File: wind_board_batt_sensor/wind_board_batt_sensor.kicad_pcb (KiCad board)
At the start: 2 copper layers, 82.4 x 23.5 mm, 35 parts, among them J1 Batt +, J2 Batt -, J3 Sys +, J4 Sys -, U1 MAX17263xxTE, U2 PTSM82903SISB2R, U3 ATtiny402-SS

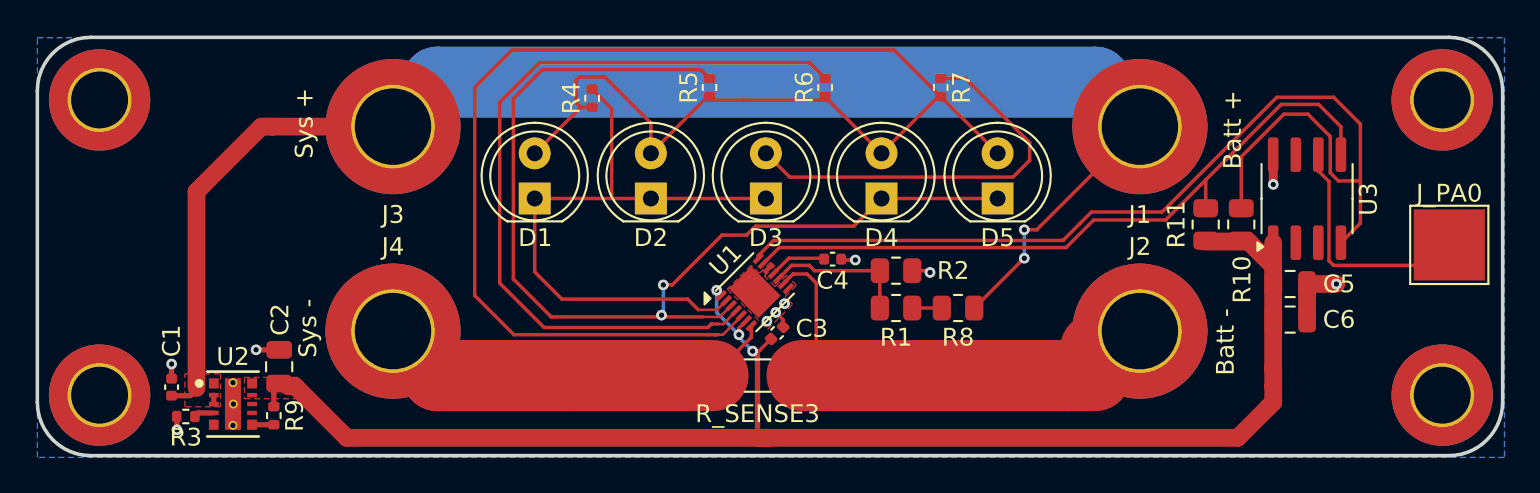
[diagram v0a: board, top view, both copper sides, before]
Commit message: All components to 0805 on battery board
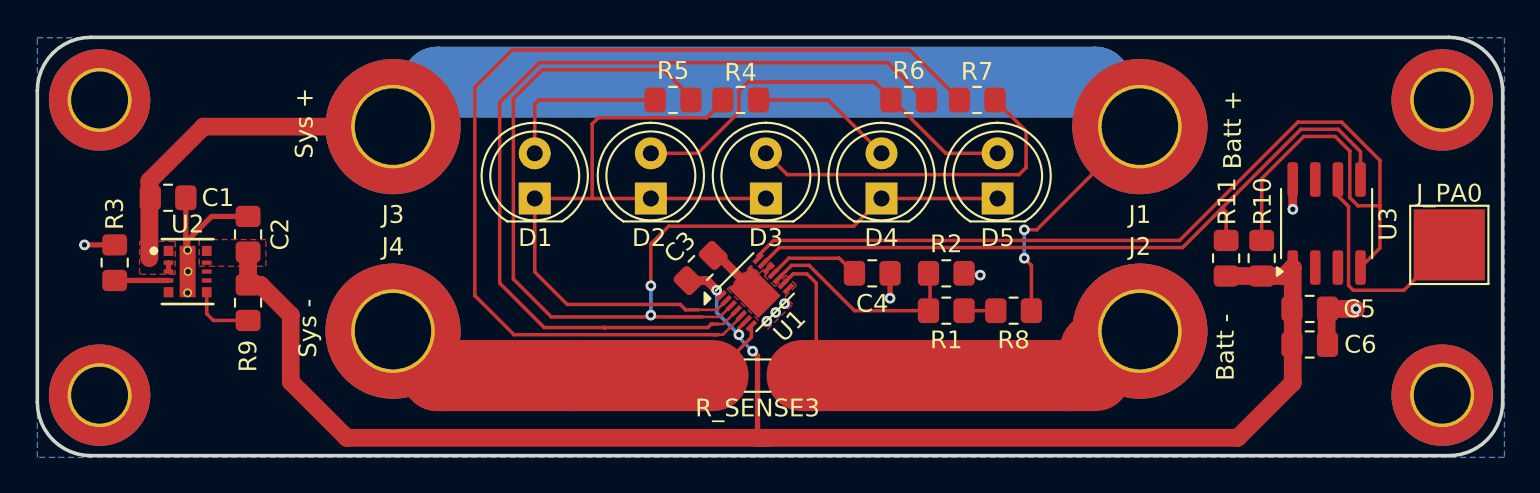
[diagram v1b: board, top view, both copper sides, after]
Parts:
- C1, C3, C4: footprint Capacitor_SMD:C_0402_1005Metric -> Resistor_SMD:R_0805_2012Metric_Pad1.20x1.40mm_HandSolder
- C2, C5, C6: footprint Capacitor_SMD:C_0805_2012Metric -> Resistor_SMD:R_0805_2012Metric_Pad1.20x1.40mm_HandSolder
- R1, R10, R11, R2, R8: footprint Resistor_SMD:R_0805_2012Metric -> Resistor_SMD:R_0805_2012Metric_Pad1.20x1.40mm_HandSolder
- R3, R4, R5, R6, R7, R9: footprint Resistor_SMD:R_0402_1005Metric -> Resistor_SMD:R_0805_2012Metric_Pad1.20x1.40mm_HandSolder
- R_SENSE3: footprint Resistor_SMD:R_1206_3216Metric -> Resistor_SMD:R_1206_3216Metric_Pad1.30x1.75mm_HandSolder
- moved C1 10.7 mm to (95.3, 99.0), turned to 0 degrees
- moved R3 9.53 mm to (92.3, 102.7), turned to 90 degrees
- moved R4 8.35 mm to (127.5, 93.5), turned to 180 degrees
- moved U2 7.87 mm to (96.5, 103.2)
- moved C2 7.65 mm to (99.8, 101.0)
- moved R9 6.51 mm to (99.8, 104.9)
- moved C3 5.64 mm to (125.3, 103.0)
- moved R6 4.75 mm to (137.0, 93.5), turned to 0 degrees
- moved R8 3.13 mm to (142.9, 105.3)
- moved R1 2.83 mm to (139.1, 105.3)
- moved R2 2.83 mm to (139.1, 103.3)
- moved C4 2.37 mm to (134.9, 103.2)
- moved R10 2.22 mm to (156.8, 102.4)
- moved R11 2.22 mm to (154.8, 102.4)
- moved R5 2.17 mm to (123.8, 93.5), turned to 0 degrees
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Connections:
- D2 pad 2: Net-(D1-A) -> Net-(D2-A)
- D4 pad 2: Net-(D1-A) -> Net-(D4-A)
- D5 pad 2: Net-(D1-A) -> Net-(D2-A)
- R4 pad 1: Net-(D1-A) -> Net-(D4-A)
- R6 pad 1: Net-(D1-A) -> Net-(D2-A)
- R7 pad 2: Net-(D1-A) -> Net-(U1-L4)
- U1 pad 5: Net-(D1-A) -> Net-(U1-L4)
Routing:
- net Net-(D1-A): track 93.8 -> 10.0 mm
- net Net-(U1-L4): track 0.00 -> 57.9 mm
- net Net-(D2-A): track 0.00 -> 23.5 mm
- net ~: track 39.2 -> 48.2 mm, vias 10 -> 8
- net Net-(D4-A): track 0.00 -> 8.31 mm
- net +3.3V: track 84.1 -> 90.8 mm
- net Net-(J1-Pin_1): track 84.3 -> 77.9 mm
- net Net-(U1-L3): track 44.5 -> 50.8 mm
- net Net-(D1-K): track 35.8 -> 41.2 mm
- net Net-(D3-A): track 23.3 -> 19.8 mm
- net Net-(U1-CELLX/CSPH): track 8.69 -> 11.9 mm
- net Net-(U2-PG): track 1.23 -> 3.69 mm
- net Net-(U1-REG): track 3.23 -> 5.27 mm
- net Net-(U2-MODE_S-CONF): track 1.15 -> 3.03 mm
- net Net-(U1-SCL): track 58.8 -> 60.5 mm
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
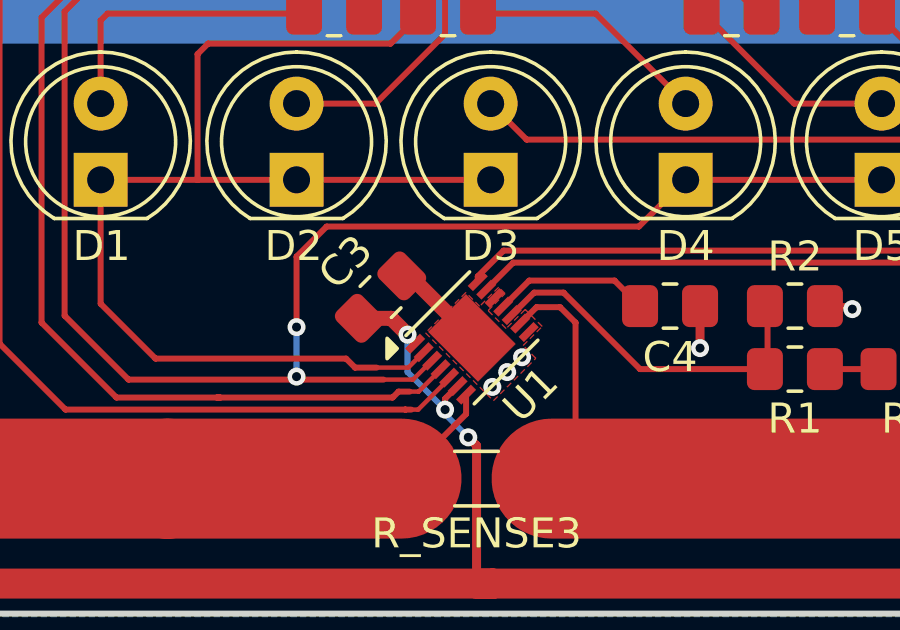
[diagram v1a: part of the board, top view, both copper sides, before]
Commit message: add vias
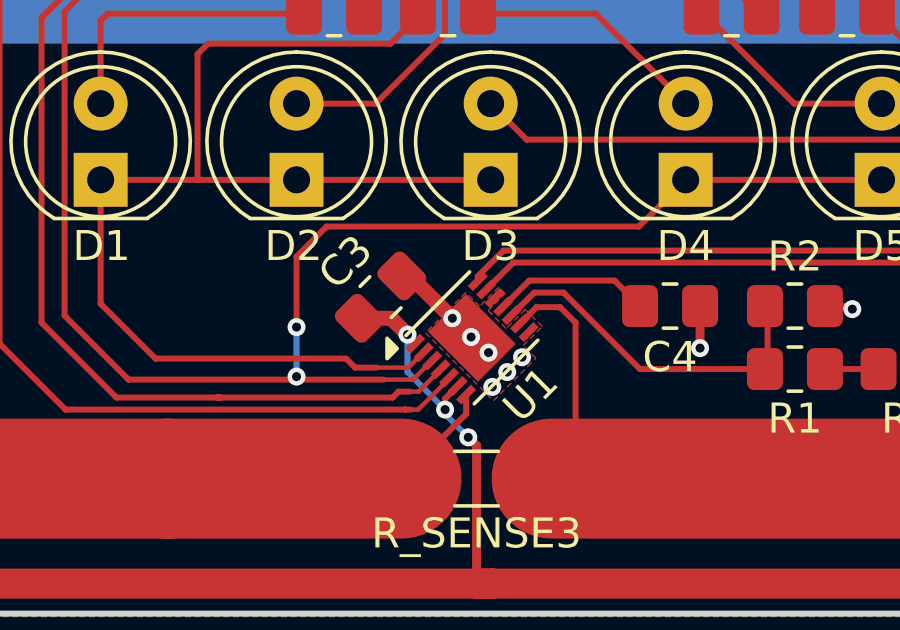
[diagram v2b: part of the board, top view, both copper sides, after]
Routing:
- net ~: track 48.2 -> 48.9 mm, vias 8 -> 11
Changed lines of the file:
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@@
+	)
+	(segment
+		(start 127.693718 103.656282)
+		(end 128.318718 104.281282)
+		(width 0.5)
+		(layer "F.Cu")
+		(net 1)
+	)
+	(segment
+		(start 128.318718 104.281282)
+		(end 128.837436 104.8)
+		(width 0.5)
+		(layer "F.Cu")
+		(net 1)
 	)
 	(segment
@@
 	(segment
 		(start 126.280328 102.242893)
-		(end 128.345925 104.30849)
+		(end 127.693718 103.656282)
 		(width 0.5)
 		(layer "F.Cu")
@@
 		(end 131.285786 103.285786)
 		(width 0.2)
+		(layer "F.Cu")
+		(net 1)
+	)
+	(segment
+		(start 128.837436 104.8)
+		(end 128.9 104.8)
+		(width 0.5)
 		(layer "F.Cu")
 		(net 1)
@@
 	)
 	(via
+		(at 128.318718 104.281282)
+		(size 0.6)
+		(drill 0.3)
+		(layers "F.Cu" "B.Cu")
+		(net 1)
+	)
+	(via
 		(at 141.025 103.35)
 		(size 0.6)
 		(drill 0.3)
+		(layers "F.Cu" "B.Cu")
+		(net 1)
+	)
+	(via
+		(at 127.693718 103.656282)
+		(size 0.6)
+		(drill 0.3)
+		(layers "F.Cu" "B.Cu")
+		(net 1)
+	)
+	(via
+		(at 128.9 104.8)
+		(size 0.6)
+		(drill 0.3)

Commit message: add silliness
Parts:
- added G***: LOGO, logos:lightning, F.Cu at (98.0, 92.8)
- added G***: LOGO, logos:more_cowbell, B.Cu at (129.3, 108.5)
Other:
- board text added: "AthleticFIELD Expansion Module Battery Meter v0.1"
- board text added: "I just want to tell you good luck. We're all counting on you."

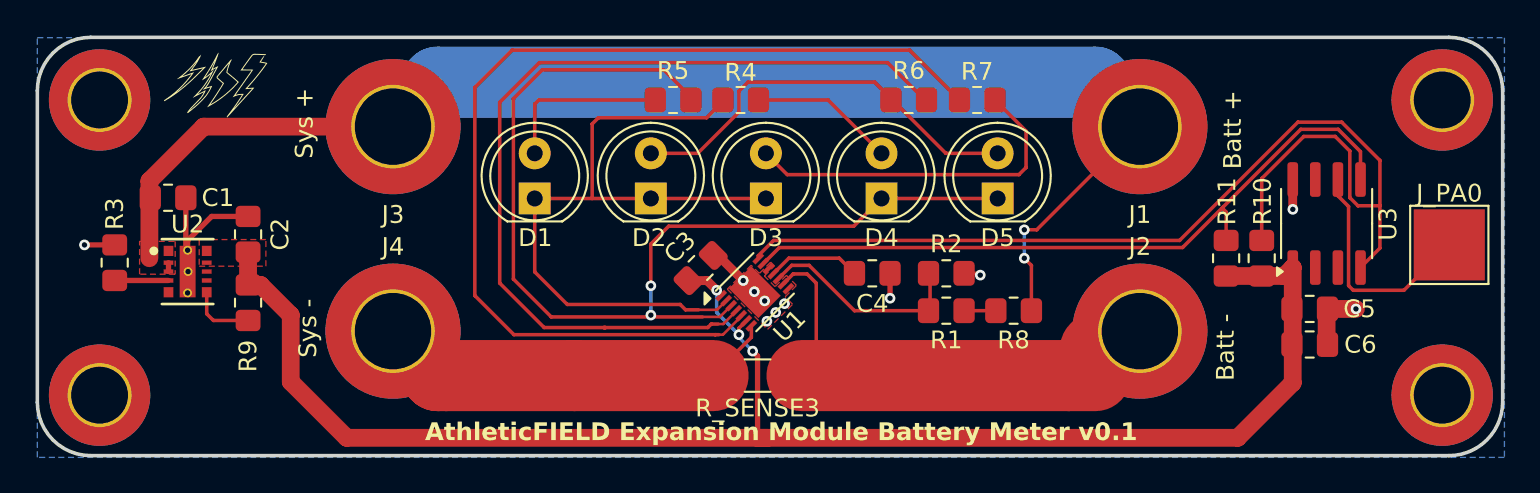
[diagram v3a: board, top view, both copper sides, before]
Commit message: swap sda-scl pins
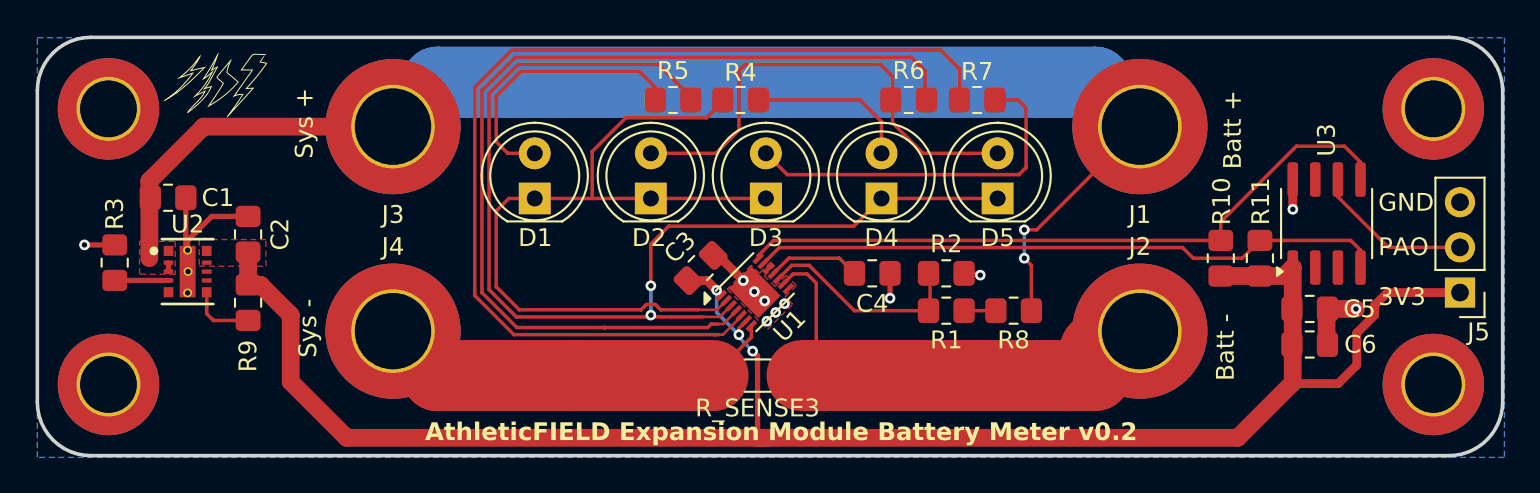
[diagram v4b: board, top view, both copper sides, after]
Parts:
- removed J_PA0: TestPoint, TestPoint:TestPoint_Pad_4.0x4.0mm
- removed the REF** at (91.5, 110.1)
- removed the REF** at (91.5, 93.5)
- removed the REF** at (167.0, 110.1)
- removed the REF** at (167.0, 93.5)
- added J5: Conn_01x03_Socket, Connector_PinHeader_2.54mm:PinHeader_1x03_P2.54mm_Vertical, F.Cu at (168.0, 104.3)
- added REF**: MountingHole_3.2mm_M3_ISO7380_Pad_TopBottom, MountingHole:MountingHole_3.2mm_M3_ISO7380_Pad_TopBottom, F.Cu at (166.5, 94.0)
- added REF**: MountingHole_3.2mm_M3_ISO7380_Pad_TopBottom, MountingHole:MountingHole_3.2mm_M3_ISO7380_Pad_TopBottom, F.Cu at (166.5, 109.5)
- added REF**: MountingHole_3.2mm_M3_ISO7380_Pad_TopBottom, MountingHole:MountingHole_3.2mm_M3_ISO7380_Pad_TopBottom, F.Cu at (92.0, 109.5)
- added REF**: MountingHole_3.2mm_M3_ISO7380_Pad_TopBottom, MountingHole:MountingHole_3.2mm_M3_ISO7380_Pad_TopBottom, F.Cu at (92.0, 94.0)
- moved R10 2.30 mm to (154.6, 102.4)
- moved R11 1.90 mm to (156.8, 102.4)
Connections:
- U3 pad 4: Net-(U1-SCL) -> Net-(U1-SDA)
- U3 pad 5: Net-(U1-SDA) -> Net-(U1-SCL)
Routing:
- net Net-(U1-SCL): track 60.5 -> 38.5 mm
- net +3.3V: track 90.8 -> 103.7 mm
- net Net-(D1-A): track 10.0 -> 15.6 mm
- net Net-(U1-SDA): track 40.7 -> 35.8 mm
- net Net-(J5-Pin_2): track 13.0 -> 9.02 mm
- net Net-(U1-L3): track 50.8 -> 54.7 mm
- net Net-(D1-K): track 41.2 -> 44.9 mm
- net Net-(D2-A): track 23.5 -> 27.1 mm
- net Net-(D4-K): track 59.6 -> 63.1 mm
- net Net-(D4-A): track 8.31 -> 9.35 mm
- net Net-(U1-L4): track 57.9 -> 58.9 mm
- net Net-(D3-A): track 19.8 -> 20.6 mm
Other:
- board text added: "3V3"
- board text added: "AthleticFIELD Expansion Module Battery Meter v0.2"
- board text added: "GND"
- board text added: "PAO"
- board text removed: "AthleticFIELD Expansion Module Battery Meter v0.1"

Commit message: add led and sca-scl header
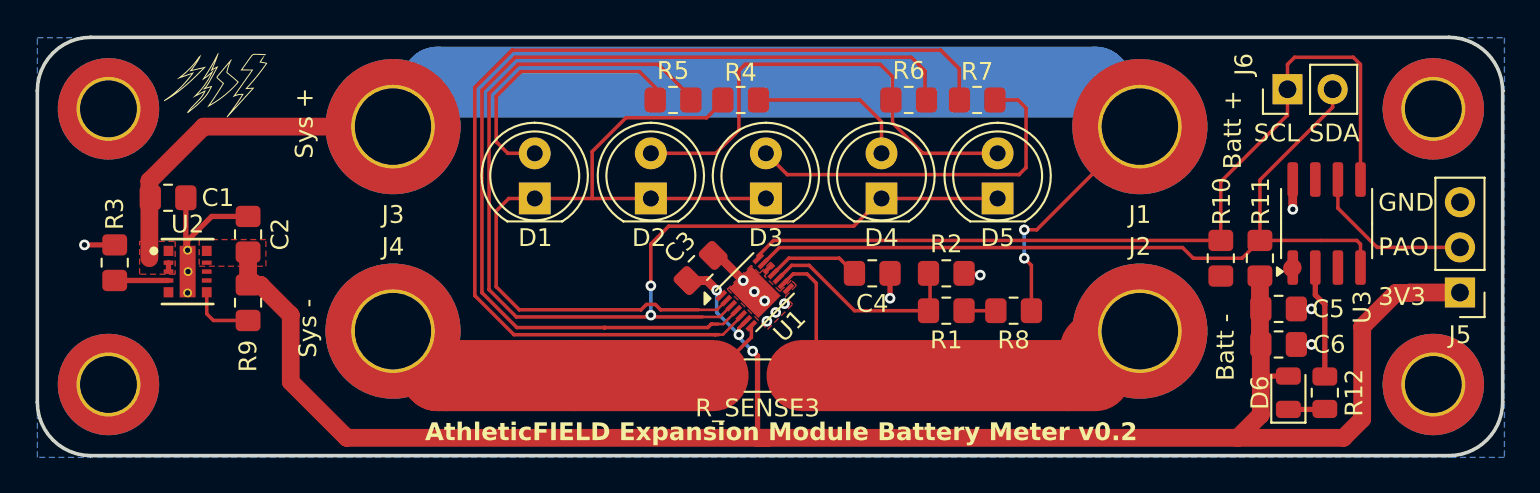
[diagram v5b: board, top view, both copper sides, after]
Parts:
- added D6: LED, LED_SMD:LED_0805_2012Metric, F.Cu at (158.3, 110.0)
- added J6: Conn_01x02_Socket, Connector_PinHeader_2.54mm:PinHeader_1x02_P2.54mm_Vertical, F.Cu at (158.3, 92.9)
- added R12: 150, Resistor_SMD:R_0805_2012Metric, F.Cu at (160.4, 110.0)
- moved C5 1.75 mm to (157.8, 105.2)
- moved C6 1.75 mm to (157.8, 107.2)
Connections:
- U2 pad 12: ~ -> (no net)
- U2 pad 13: ~ -> (no net)
- U2 pad 14: ~ -> (no net)
- U3 pad 2: unconnected-(U3-PA6-Pad2) -> Net-(U3-PA6)
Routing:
- net Net-(J6-Pin_2): track 35.8 -> 46.2 mm
- net Net-(J6-Pin_1): track 38.5 -> 48.9 mm
- net Net-(U3-PA6): track 0.00 -> 6.35 mm
- net +3.3V: track 103.7 -> 106.5 mm
- net Net-(D6-K): track 0.00 -> 2.06 mm
- net ~: track 48.9 -> 47.2 mm, vias 11 -> 12
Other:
- board text added: "SCL"
- board text added: "SDA"

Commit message: fix stuff
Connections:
- J5 pad 2: Net-(J5-Pin_2) -> ~
- J5 pad 3: ~ -> Net-(J5-Pin_3)
- U3 pad 6: Net-(J5-Pin_2) -> Net-(J5-Pin_3)
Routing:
- net Net-(J5-Pin_2): track 9.39 -> 0.00 mm
- net Net-(J5-Pin_3): track 0.00 -> 7.96 mm
- net +3.3V: track 106.5 -> 110.7 mm
